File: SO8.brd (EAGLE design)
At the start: 9 parts

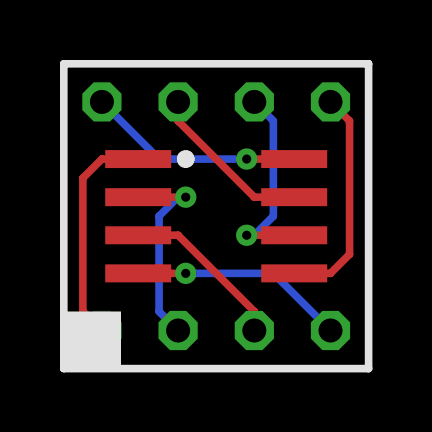
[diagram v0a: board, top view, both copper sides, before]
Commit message: adjusted trace widths
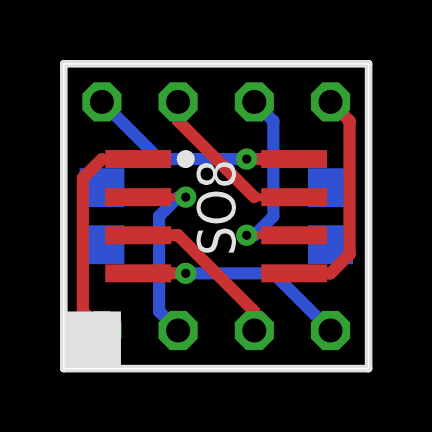
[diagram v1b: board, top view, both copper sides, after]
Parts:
- added E$1, E$2: (no value), ref-packages:C0805
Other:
- board outline added: 10.2 x 10.2 mm
- board text added: "SO8"
